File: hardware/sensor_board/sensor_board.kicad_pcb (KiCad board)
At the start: 2 copper layers, 70 x 30 mm, 3 parts, among them J1 I2C Connector, U1 CJMCU-3935, U2 BME280

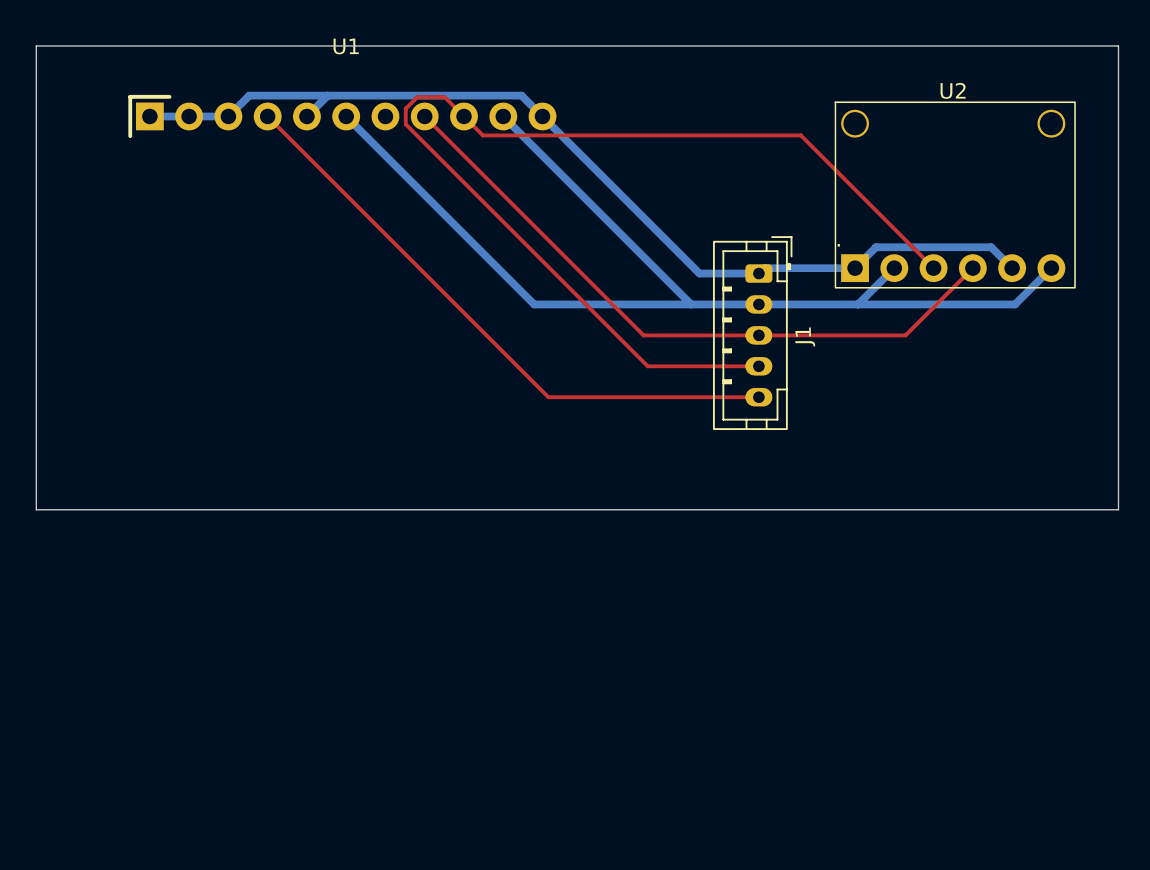
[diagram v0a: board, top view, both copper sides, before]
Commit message: hw v1 battery selection
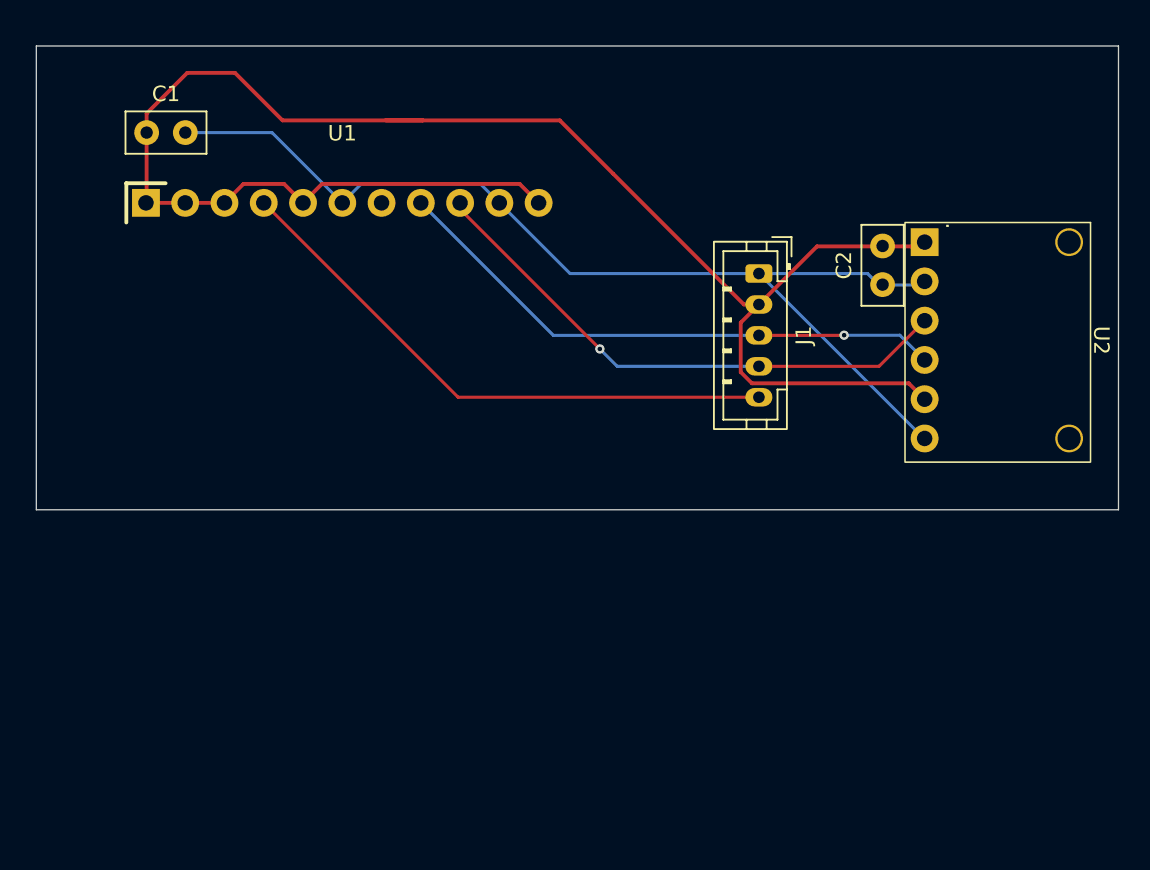
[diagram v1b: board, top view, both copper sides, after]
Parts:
- added C1: 100nf, Capacitor_THT:C_Disc_D5.0mm_W2.5mm_P2.50mm, F.Cu at (166.1, 36.6)
- added C2: 100nf, Capacitor_THT:C_Disc_D5.0mm_W2.5mm_P2.50mm, F.Cu at (213.7, 46.4)
- moved U1 5.59 mm to (178.8, 41.1)
- moved U2 4.81 mm to (216.5, 43.7), turned to -90 degrees
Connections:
- J1 pad 1: +3V3 -> GND
- J1 pad 2: GND -> +3V3
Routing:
- net +3V3: track 64.3 -> 112.4 mm
- net /I2C_SCL: track 69.4 -> 35.9 mm, vias 0 -> 1
- net /I2C_SDA: track 43.1 -> 36.8 mm, vias 0 -> 1
- net GND: track 72.1 -> 68.1 mm
- net /WAKE_IRQ: track 39.3 -> 37.2 mm

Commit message: soft v1
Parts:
- moved C1 2.52 mm to (168.7, 36.6), turned to 180 degrees
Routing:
- net +3V3: track 112.4 -> 109.9 mm
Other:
- board size 70 x 30 mm -> 70 x 50 mm
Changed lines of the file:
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@@
 	(footprint "Capacitor_THT:C_Disc_D5.0mm_W2.5mm_P2.50mm"
 		(layer "F.Cu")
-		(at 166.136 36.6014)
+		(at 168.656 36.6014 180)
 		(descr "C, Disc series, Radial, pin pitch=2.50mm, diameter*width=5*2.5mm^2, Capacitor, http://cdn-reichelt.de/documents/datenblatt/B300/DS_KERKO_TC.pdf")
 		(tags "C Disc series Radial pin pitch 2.50mm diameter 5mm width 2.5mm Capacitor")
@@
 		(duplicate_pad_numbers_are_jumpers no)
 		(fp_line
-			(start -1.37 -1.37)
-			(end 3.87 -1.37)
+			(start 3.87 1.37)
+			(end -1.37 1.37)
+			(stroke
+				(width 0.12)
+				(type solid)
+			)
+			(layer "F.SilkS")
+		)
+		(fp_line
+			(start 3.87 -1.37)
+			(end 3.87 1.37)
 			(stroke
 				(width 0.12)
@@
 		)
 		(fp_line
-			(start 3.87 -1.37)
-			(end 3.87 1.37)
-			(stroke
-				(width 0.12)
-				(type solid)
-			)
-			(layer "F.SilkS")
-		)
-		(fp_line
-			(start 3.87 1.37)
-			(end -1.37 1.37)
+			(start -1.37 -1.37)
+			(end 3.87 -1.37)
 			(stroke
 				(width 0.12)
@@
 		)
 		(pad "1" thru_hole circle
-			(at 0 0)
+			(at 0 0 180)
 			(size 1.6 1.6)
 			(drill 0.8)
@@
 		)
 		(pad "2" thru_hole circle
-			(at 2.5 0)
+			(at 2.5 0 180)
 			(size 1.6 1.6)
 			(drill 0.8)
@@
 	)
 	(gr_rect
-		(start 159 31)
-		(end 229 61)
+		(start 158.675 32.258)
+		(end 228.675 82.258)
 		(stroke
 			(width 0.05)
-			(type default)
+			(type solid)
 		)
 		(fill no)
@@
 	)
 	(segment
+		(start 183.9976 35.814)
+		(end 174.9298 35.814)
+		(width 0.25)
+		(layer "F.Cu")
+		(net "+3V3")
+	)
+	(segment
 		(start 175.0256 39.923)
 		(end 176.2506 41.148)
@@
 	)
 	(segment
+		(start 166.156 41.0826)
+		(end 166.0906 41.148)
+		(width 0.25)
+		(layer "F.Cu")
+		(net "+3V3")
+	)
+	(segment
 		(start 204.7682 47.72)
 		(end 196.3166 39.2684)
@@
 	)
 	(segment
-		(start 166.136 41.1026)
-		(end 166.0906 41.148)
-		(width 0.25)
-		(layer "F.Cu")
-		(net "+3V3")
-	)
-	(segment
 		(start 216.187 43.962)
 		(end 216.461 43.688)
@@
 	)
 	(segment
-		(start 183.9976 35.814)
-		(end 174.9298 35.814)
-		(width 0.25)
-		(layer "F.Cu")
-		(net "+3V3")
-	)
-	(segment
 		(start 190.2656 39.923)
 		(end 191.4906 41.148)
@@
 	)
 	(segment
+		(start 167.8324 34.925)
+		(end 166.156 36.6014)
+		(width 0.25)
+		(layer "F.Cu")
+		(net "+3V3")
+	)
+	(segment
+		(start 174.9298 35.814)
+		(end 174.0408 34.925)
+		(width 0.25)
+		(layer "F.Cu")
+		(net "+3V3")
+	)
+	(segment
 		(start 213.5124 43.962)
 		(end 216.187 43.962)
@@
 	)
 	(segment
+		(start 174.0408 34.925)
+		(end 167.8324 34.925)
+		(width 0.25)
+		(layer "F.Cu")
+		(net "+3V3")
+	)
+	(segment
 		(start 196.3166 39.2684)
 		(end 192.8622 35.814)
@@
 	)
 	(segment
-		(start 174.9298 35.814)
-		(end 171.8564 32.7406)
-		(width 0.25)
-		(layer "F.Cu")
-		(net "+3V3")
-	)
-	(segment
-		(start 171.8564 32.7406)
-		(end 168.7576 32.7406)
-		(width 0.25)
-		(layer "F.Cu")
-		(net "+3V3")
-	)
-	(segment
-		(start 166.136 35.3622)
-		(end 166.136 36.6014)
-		(width 0.25)
-		(layer "F.Cu")
-		(net "+3V3")
-	)
-	(segment
-		(start 168.7576 32.7406)
-		(end 166.136 35.3622)
-		(width 0.25)
-		(layer "F.Cu")
-		(net "+3V3")
-	)
-	(segment
-		(start 166.136 36.6014)
-		(end 166.136 41.1026)
-		(width 0.25)
-		(layer "F.Cu")
+		(start 166.156 36.6014)
+		(end 166.156 41.0826)
+		(width 0.25)
+		(layer "F.Cu")
